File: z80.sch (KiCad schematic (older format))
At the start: 0 parts

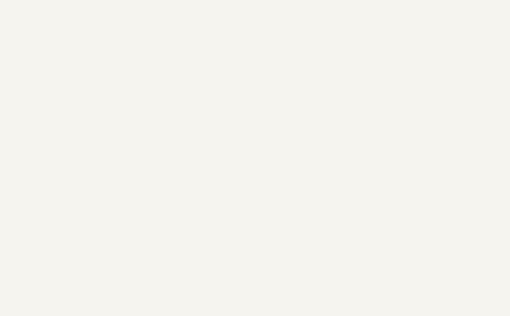
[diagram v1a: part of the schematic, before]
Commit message: Removed the interrupt priority circuitry
After second thought the added complexity just wasn't worth it.
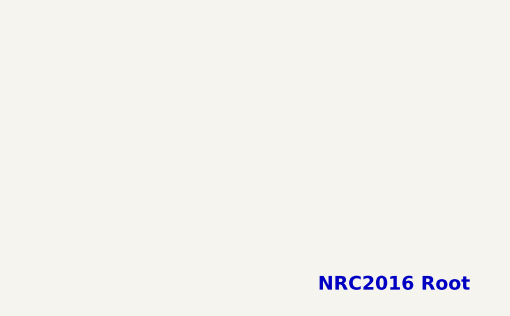
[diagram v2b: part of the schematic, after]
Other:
- note added: "NRC2016 Root"
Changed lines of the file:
@@
 Entry Wire Line
 	3950 5700 4050 5800
+Text Notes 7350 7500 0    60   ~ 12
+NRC2016 Root
 $EndSCHEMATC

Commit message: Updated LEDs, added power supply options, added mounting holes in schematic.
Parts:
- added C? (x2): 100u, symbol CP
- added C?: 330u, symbol CP
- added C? (x2): 10u, symbol CP
- added CON? (x2): BARREL_JACK, symbol BARREL_JACK
- added D? (x4): 11DQ06, symbol D_Schottky
- added D?: LED, LEDs:LED-3MM, symbol LED
- added L?: 330uH / 1A, symbol INDUCTOR
- added MH? (x4): MH_3mm, symbol MH_3mm
- added P?: USB_B, symbol USB_B
- added R?: 220, Resistors_SMD:R_0805_HandSoldering, symbol R
- added U?: TL2575-5, symbol TL2575-5
- added U?: LM7805CT, TO-220, symbol LM7805CT
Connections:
- net labels added: GND, VCC
- wire segments 95 -> 139
- no-connect marks 0 -> 3
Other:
- note added: "1N5819 will probably also work."
- note added: "Linear power supply"
- note added: "Mounting holes"
- note added: "Power indicator"
- note added: "Switch-mode power supply"
- note added: "USB power source"

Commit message: Update PCB, better layout. Got Addr bus back in order
Think having both USB and DC input would be useful. Switchmode a plus
then plugpack/battery etc voltage doesn't matter. Plus I have a bag full
of those parts too!

I've refdes'd the linear reg just to deal with the net. Will remove if
we both are happy with switcher. Linear cheaper to kit out I guess.

Was trying to find a better way to combine USB and DC power rails than
just schottky diodes. If you have any ideas.

Going to have a big area under the IO ports, might be worth adding a USB
to serial, or sacrifice a IO port for some blinky LEDs and buttons?
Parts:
- added D12, D9: 11DQ06, Diodes_SMD:DO-214AB_Handsoldering, symbol D_Schottky
- C1003, C1004: renamed from C?; footprint (none) -> Capacitors_SMD:C_0201
- C11: renamed from C?; footprint (none) -> Capacitors_SMD:c_elec_4x5.3
- C12, C13: renamed from C?; footprint (none) -> Capacitors_SMD:c_elec_6.3x4.5
- CON1, CON1002: renamed from CON?; footprint (none) -> Connect:BARREL_JACK
- D1: renamed from D?; footprint LEDs:LED-3MM -> LEDs:LED_1206
- D10, D11: renamed from D?; footprint (none) -> Diodes_SMD:DO-214AB_Handsoldering
- D1003, D1004: renamed from D?; footprint (none) -> Diodes_SMD:DO-214AB
- L1: renamed from L?; footprint (none) -> Inductors_NEOSID:Neosid_Inductor_SM-PIC1004H
- MH1, MH2, MH3, MH4: renamed from MH?; footprint (none) -> Mounting_Holes:MountingHole_3.2mm_M3
- U1001: renamed from U?; footprint (none) -> TO_SOT_Packages_SMD:TO-263-5Lead
- U1002: renamed from U?; footprint TO-220 -> Power_Integrations:TO-220
- USB1: renamed from P?; footprint (none) -> Connect:USB_B
- gave numbers to parts that had none: 1
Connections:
- wire segments 139 -> 142

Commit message: PCB layout complete, passes DRC, more tuning required
One thing not enough buffers for all address lines (missed A5), so
swapped out the CLK. Not sure if that was a good idea, but didn't want
to add another chip for a single buffer. :(
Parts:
- removed C1003: 100u, Capacitors_SMD:C_0201, symbol CP
- removed C1004: 10u, Capacitors_SMD:C_0201, symbol CP
- removed C12: 100u, Capacitors_SMD:c_elec_6.3x4.5, symbol CP
- removed C13: 330u, Capacitors_SMD:c_elec_6.3x4.5, symbol CP
- removed CON1, CON1002: BARREL_JACK, Connect:BARREL_JACK, symbol BARREL_JACK
- removed D10, D11, D12, D9: 11DQ06, Diodes_SMD:DO-214AB_Handsoldering, symbol D_Schottky
- removed D1003, D1004: 11DQ06, Diodes_SMD:DO-214AB, symbol D_Schottky
- removed L1: 330uH / 1A, Inductors_NEOSID:Neosid_Inductor_SM-PIC1004H, symbol INDUCTOR
- removed U1001: TL2575-5, TO_SOT_Packages_SMD:TO-263-5Lead, symbol TL2575-5
- removed U1002: LM7805CT, Power_Integrations:TO-220, symbol LM7805CT
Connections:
- wire segments 142 -> 104
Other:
- note removed: "1N5819 will probably also work."
- note removed: "Linear power supply"
- note removed: "Switch-mode power supply"
- moved on the sheet: C11, D1, R21, USB1

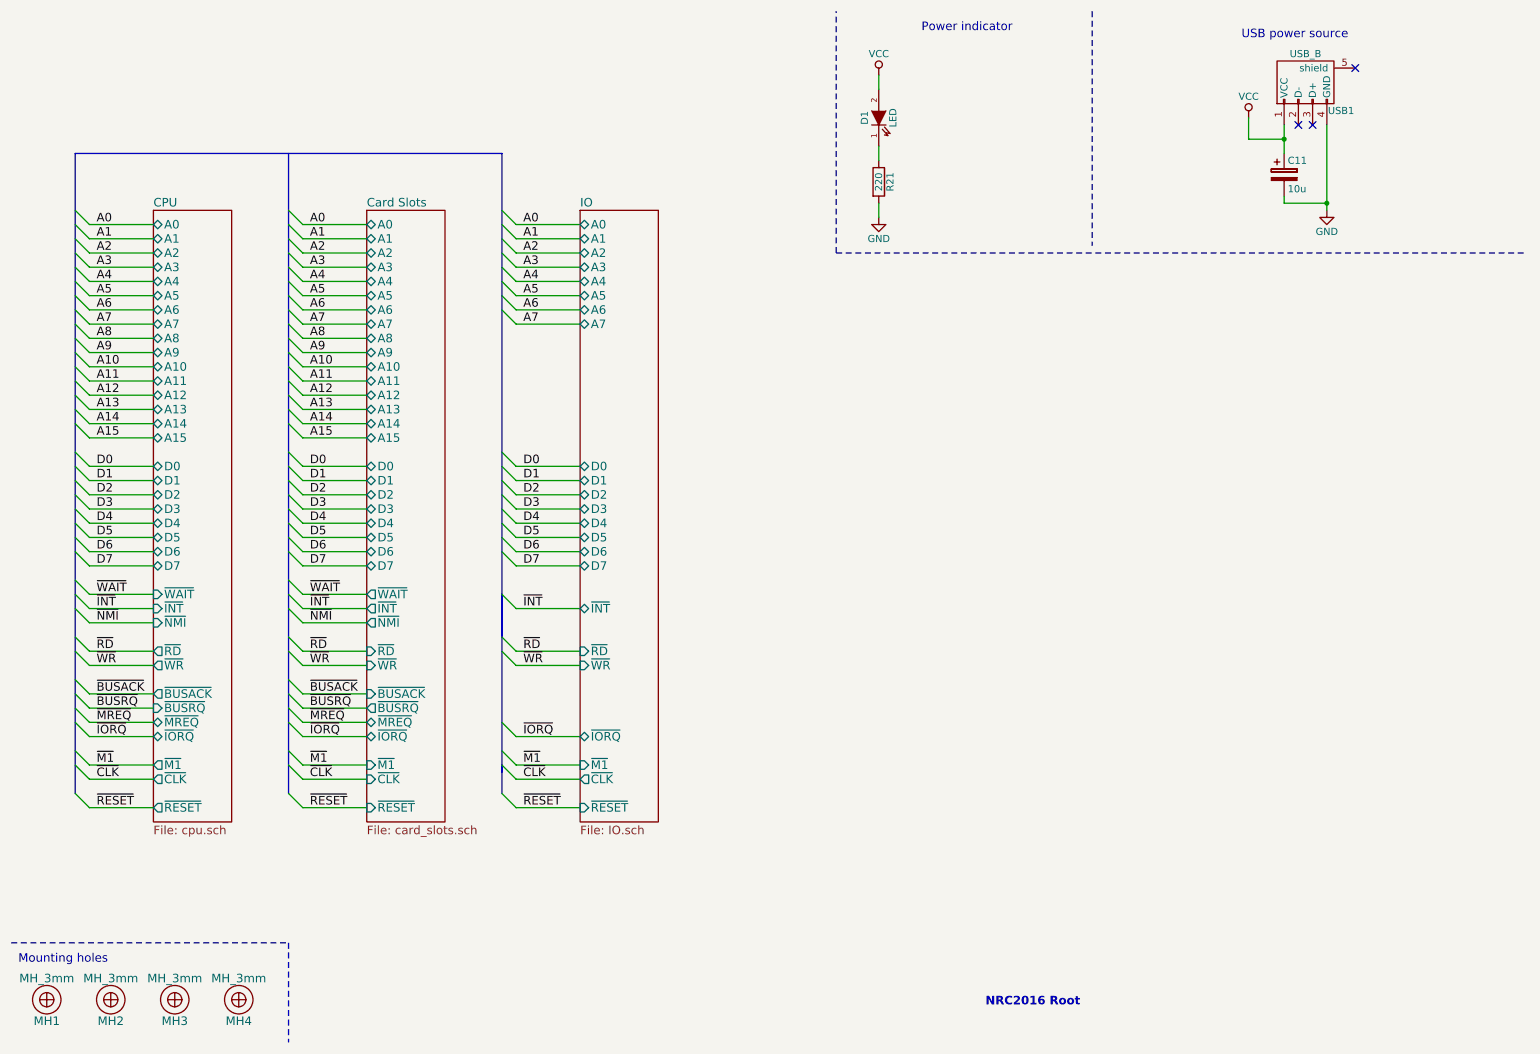
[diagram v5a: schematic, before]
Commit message: Update with smaller board and through-hole parts.
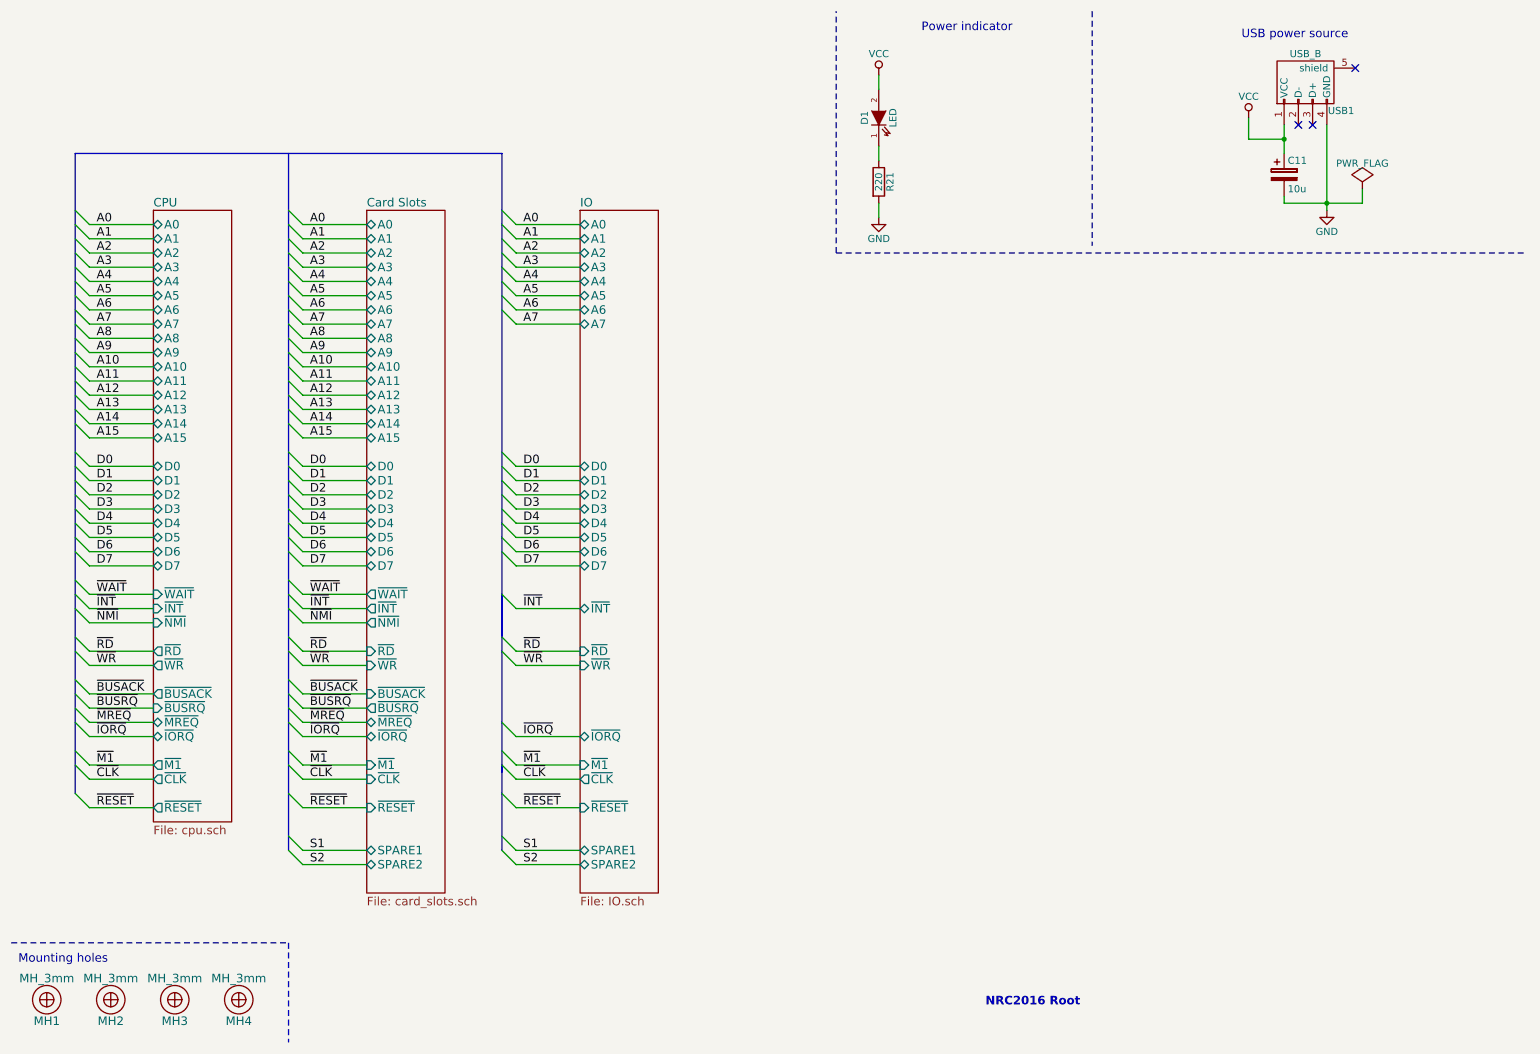
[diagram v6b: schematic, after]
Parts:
- C11: footprint Capacitors_SMD:c_elec_4x5.3 -> Capacitors_ThroughHole:C_Radial_D6.3_L11.2_P2.5
- D1: footprint LEDs:LED_1206 -> LEDs:LED-3MM
- R21: footprint Resistors_SMD:R_0805_HandSoldering -> Resistors_ThroughHole:Resistor_Horizontal_RM7mm
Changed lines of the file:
@@
 $Descr A4 11693 8268
 encoding utf-8
-Sheet 1 16
+Sheet 1 11
 Title ""
 Date ""
@@
 ~NMI
 $Sheet
-S 4500 1900 550  4300
+S 4500 1900 550  4800
 U 578460AE
 F0 "IO" 60
@@
 F23 "~CLK" O L 4500 5900 60
 F24 "~RESET" I L 4500 6100 60
+F25 "SPARE1" B L 4500 6400 60
+F26 "SPARE2" B L 4500 6500 60
 $EndSheet
 Entry Wire Line
@@
 	2550 4400 3000 4400
 Wire Bus Line
-	2450 1500 2450 6000
+	2450 1500 2450 6400
 Wire Wire Line
 	2550 4600 3000 4600
@@
 	3950 2000 4050 2100
 $Sheet
-S 3000 1900 550  4300
+S 3000 1900 550  4800
 U 577F17CE
 F0 "Card Slots" 60
@@
 F36 "~RESET" I L 3000 6100 60
 F37 "~NMI" O L 3000 4800 60
+F38 "SPARE1" B L 3000 6400 60
+F39 "SPARE2" B L 3000 6500 60
 $EndSheet
 Wire Wire Line
@@
 	3950 4900 4050 5000
 Wire Bus Line
-	3950 5800 3950 6000
+	3950 5800 3950 6400
 Wire Wire Line
 	4050 6100 4500 6100
@@
 F 0 "C11" H 9475 1750 50  0000 L CNN
 F 1 "10u" H 9475 1550 50  0000 L CNN
-F 2 "Capacitors_SMD:c_elec_4x5.3" H 9488 1500 50  0001 C CNN
+F 2 "Capacitors_ThroughHole:C_Radial_D6.3_L11.2_P2.5" H 9488 1500 50  0001 C CNN
 F 3 "" H 9450 1650 50  0000 C CNN
 	1    9450 1650
@@
 	9450 1800 9450 1850
 Wire Wire Line
-	9450 1850 9750 1850
+	9450 1850 10000 1850
 Connection ~ 9750 1850
 NoConn ~ 9550 1300
@@
 F 0 "D1" H 6600 1350 50  0000 C CNN
 F 1 "LED" H 6600 1150 50  0000 C CNN
-F 2 "LEDs:LED_1206" H 6600 1250 50  0001 C CNN
+F 2 "LEDs:LED-3MM" H 6600 1250 50  0001 C CNN
 F 3 "" H 6600 1250 50  0000 C CNN
 	1    6600 1250
@@
 F 0 "R21" V 6680 1700 50  0000 C CNN
 F 1 "220" V 6600 1700 50  0000 C CNN
-F 2 "Resistors_SMD:R_0805_HandSoldering" V 6530 1700 50  0001 C CNN
+F 2 "Resistors_ThroughHole:Resistor_Horizontal_RM7mm" V 6530 1700 50  0001 C CNN
 F 3 "" H 6600 1700 50  0000 C CNN
 	1    6600 1700
@@
 Text Notes 6900 650  0    60   ~ 0
 Power indicator
-Wire Wire Line
-	9200 1400 9450 1400
 Wire Notes Line
 	6300 2200 6300 500
 Wire Wire Line
 	9200 1250 9200 1400
+Wire Wire Line
+	4050 6500 4500 6500
+Text Label 4100 6500 0    60   ~ 0
+S2
+Entry Wire Line
+	3950 6400 4050 6500
+Wire Wire Line
+	4050 6400 4500 6400
+Text Label 4100 6400 0    60   ~ 0
+S1
+Entry Wire Line
+	3950 6300 4050 6400
+Wire Wire Line
+	2550 6500 3000 6500
+Text Label 2600 6500 0    60   ~ 0
+S2
+Entry Wire Line
+	2450 6400 2550 6500
+Wire Wire Line
+	2550 6400 3000 6400
+Text Label 2600 6400 0    60   ~ 0
+S1
+Entry Wire Line
+	2450 6300 2550 6400
+$Comp
+L PWR_FLAG #FLG05
+U 1 1 57951B7E
+P 10000 1750
+F 0 "#FLG05" H 10000 1845 50  0001 C CNN
+F 1 "PWR_FLAG" H 10000 1930 50  0000 C CNN
+F 2 "" H 10000 1750 50  0000 C CNN
+F 3 "" H 10000 1750 50  0000 C CNN
+	1    10000 1750
+	1    0    0    -1
+$EndComp
+Wire Wire Line
+	10000 1850 10000 1750
+Wire Wire Line
+	9200 1400 9450 1400
 $EndSCHEMATC

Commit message: New layout complete. Now with rc2014 compat. slots!
Plus on board address decoding, single stepping using M1 line so button
is click per instruction. Board is also much smaller!
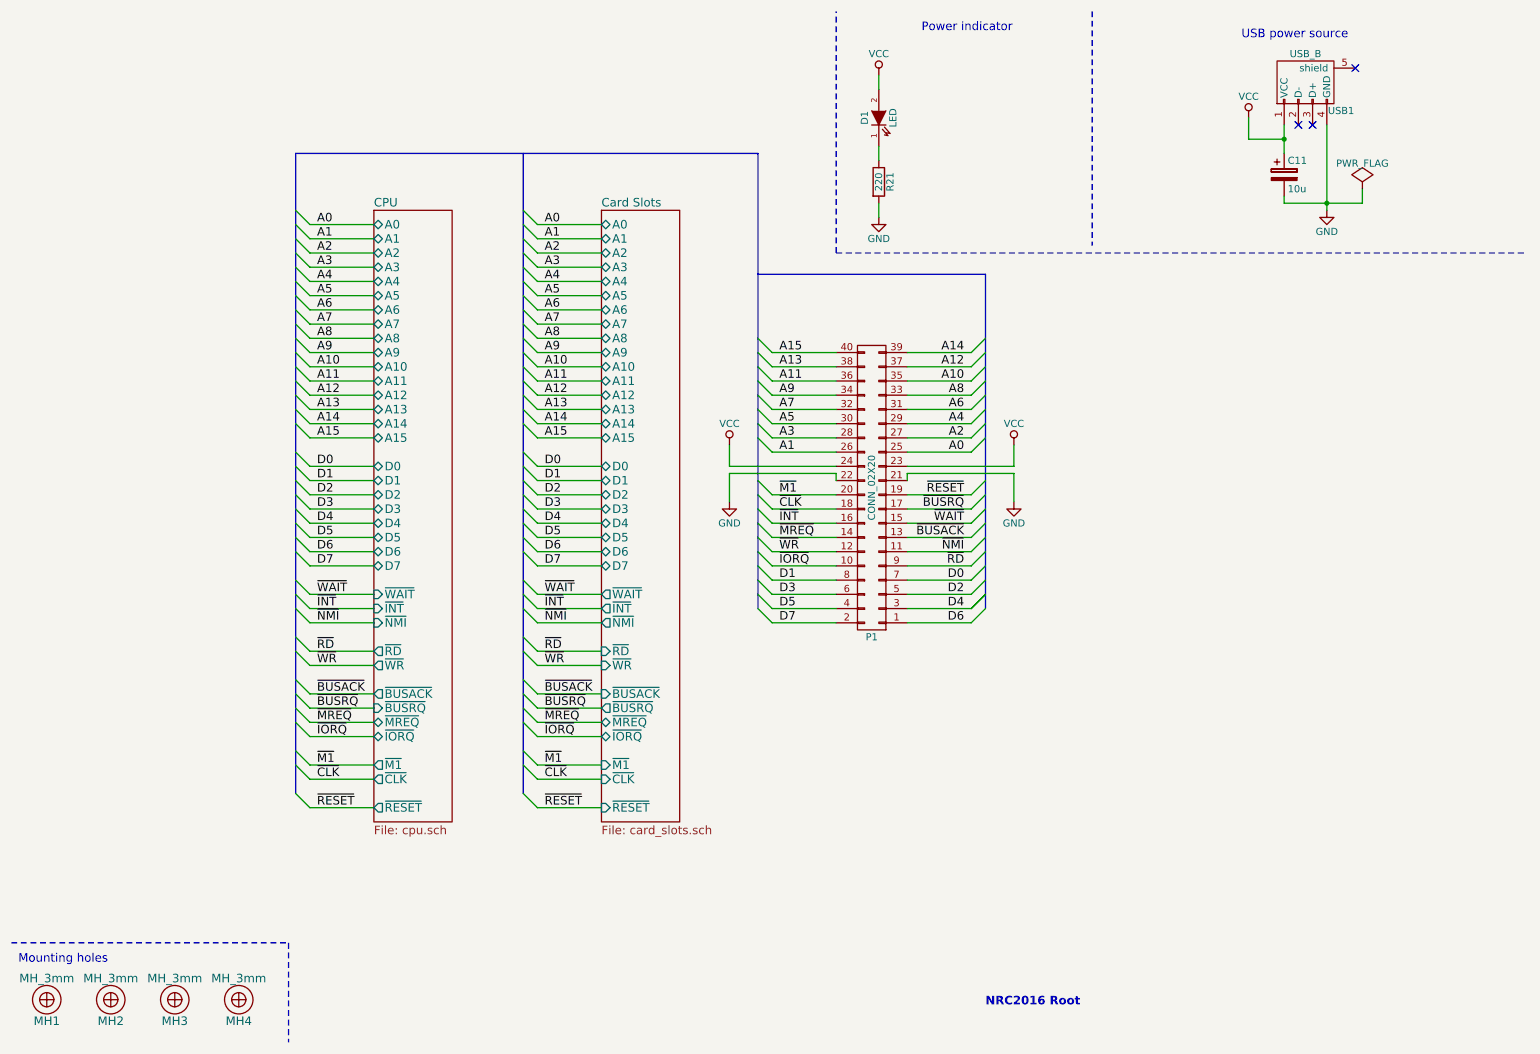
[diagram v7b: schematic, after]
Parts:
- added P1: CONN_02X20, Socket_Strips:Socket_Strip_Angled_2x20, symbol CONN_02X20
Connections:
- net A0: now also P1.25 (P25)
- net A1: now also P1.26 (P26)
- net A10: now also P1.35 (P35)
- net A11: now also P1.36 (P36)
- net A12: now also P1.37 (P37)
- net A13: now also P1.38 (P38)
- net A14: now also P1.39 (P39)
- net A15: now also P1.40 (P40)
- net A2: now also P1.27 (P27)
- net A3: now also P1.28 (P28)
- net A4: now also P1.29 (P29)
- net A5: now also P1.30 (P30)
- net A6: now also P1.31 (P31)
- net A7: now also P1.32 (P32)
- net A8: now also P1.33 (P33)
- net A9: now also P1.34 (P34)
- net D0: now also P1.7 (P7)
- net D1: now also P1.8 (P8)
- net D2: now also P1.5 (P5)
- net D3: now also P1.6 (P6)
- net D4: now also P1.3 (P3)
- net D5: now also P1.4 (P4)
- net D6: now also P1.1 (P1)
- net D7: now also P1.2 (P2)
- net GND: now also P1.21 (P21), P1.22 (P22)
- net VCC: now also P1.23 (P23), P1.24 (P24)
- net ~BUSACK: now also P1.13 (P13)
- net ~BUSRQ: now also P1.17 (P17)
- net ~CLK: now also P1.18 (P18)
- net ~INT: now also P1.16 (P16)
- net ~IORQ: now also P1.10 (P10)
- net ~M1: now also P1.20 (P20)
- net ~MREQ: now also P1.14 (P14)
- net ~NMI: now also P1.11 (P11)
- net ~RD: now also P1.9 (P9)
- net ~RESET: now also P1.19 (P19)
- net ~WAIT: now also P1.15 (P15)
- net ~WR: now also P1.12 (P12)

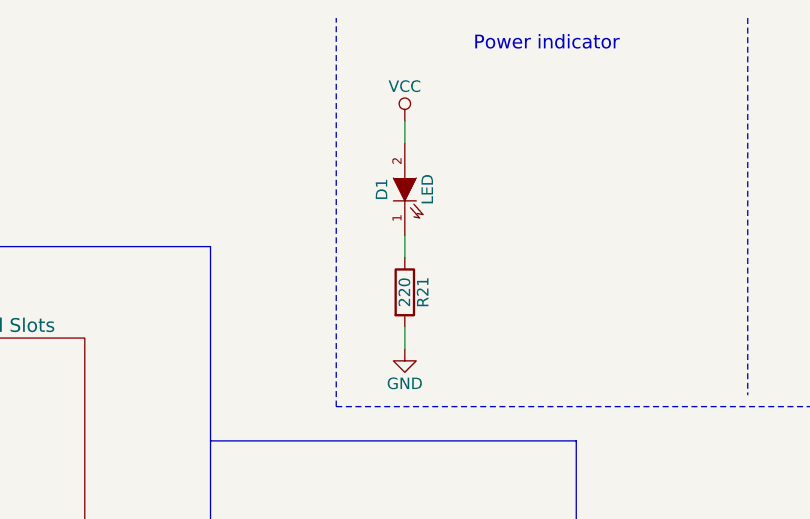
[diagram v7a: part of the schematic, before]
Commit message: Another new board layout. Few tidy ups.
Removed the single step circuit, not worth the board space and headache.
Added legend for the IO slot for easy reference. Still toying where to
put the power LED, annoying me with that resistor. Think I'm happy with
it now. Spaced things out a little to make it easy for manufacture, made
sure no traces are near board edges as much as possible.
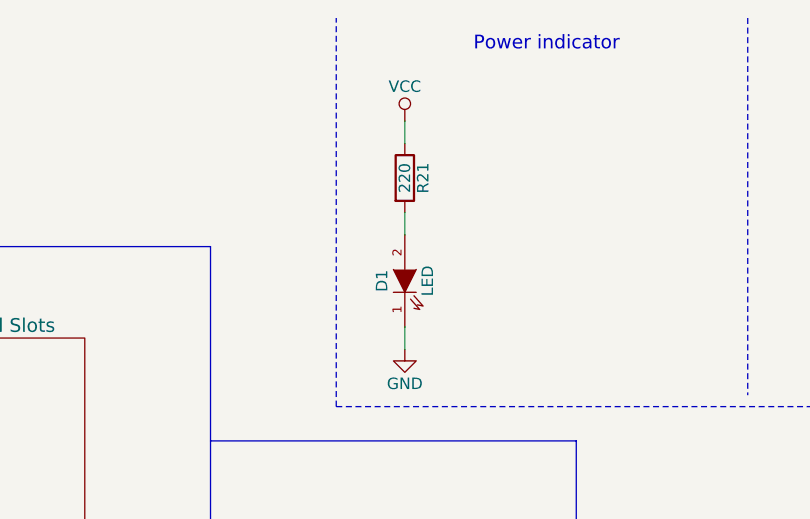
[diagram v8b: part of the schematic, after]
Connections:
- net GND: now also D1.1 (K); no longer R21.2
- net VCC: now also R21.1; no longer D1.2 (A)
- new net: D1.2 (A), R21.2
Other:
- moved on the sheet: D1, R21
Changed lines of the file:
@@
 L LED D1
 U 1 1 5799296C
-P 6600 1250
-F 0 "D1" H 6600 1350 50  0000 C CNN
-F 1 "LED" H 6600 1150 50  0000 C CNN
-F 2 "LEDs:LED-3MM" H 6600 1250 50  0001 C CNN
-F 3 "" H 6600 1250 50  0000 C CNN
-	1    6600 1250
+P 6600 1650
+F 0 "D1" H 6600 1750 50  0000 C CNN
+F 1 "LED" H 6600 1550 50  0000 C CNN
+F 2 "LEDs:LED-3MM" H 6600 1650 50  0001 C CNN
+F 3 "" H 6600 1650 50  0000 C CNN
+	1    6600 1650
 	0    -1   -1   0
 $EndComp
@@
 L R R21
 U 1 1 57992973
-P 6600 1700
-F 0 "R21" V 6680 1700 50  0000 C CNN
-F 1 "220" V 6600 1700 50  0000 C CNN
-F 2 "Resistors_ThroughHole:Resistor_Horizontal_RM7mm" V 6530 1700 50  0001 C CNN
-F 3 "" H 6600 1700 50  0000 C CNN
-	1    6600 1700
+P 6600 1200
+F 0 "R21" V 6680 1200 50  0000 C CNN
+F 1 "220" V 6600 1200 50  0000 C CNN
+F 2 "Resistors_ThroughHole:Resistor_Horizontal_RM7mm" V 6530 1200 50  0001 C CNN
+F 3 "" H 6600 1200 50  0000 C CNN
+	1    6600 1200
 	1    0    0    -1
 $EndComp
@@
 $EndComp
 Wire Wire Line
-	6600 1450 6600 1550
+	6600 1350 6600 1450
 Wire Wire Line
 	6600 1850 6600 1950
